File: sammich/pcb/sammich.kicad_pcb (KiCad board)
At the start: 2 copper layers, 34.5 x 25.9 mm, 38 parts, among them J1 Conn_01x02, J2 Conn_02x05_Odd_Even, J3 Conn_01x04, U1 STM32F103RBTx, U2 LD3985M33R_SOT23, U3 MAX485E, Y1 Crystal

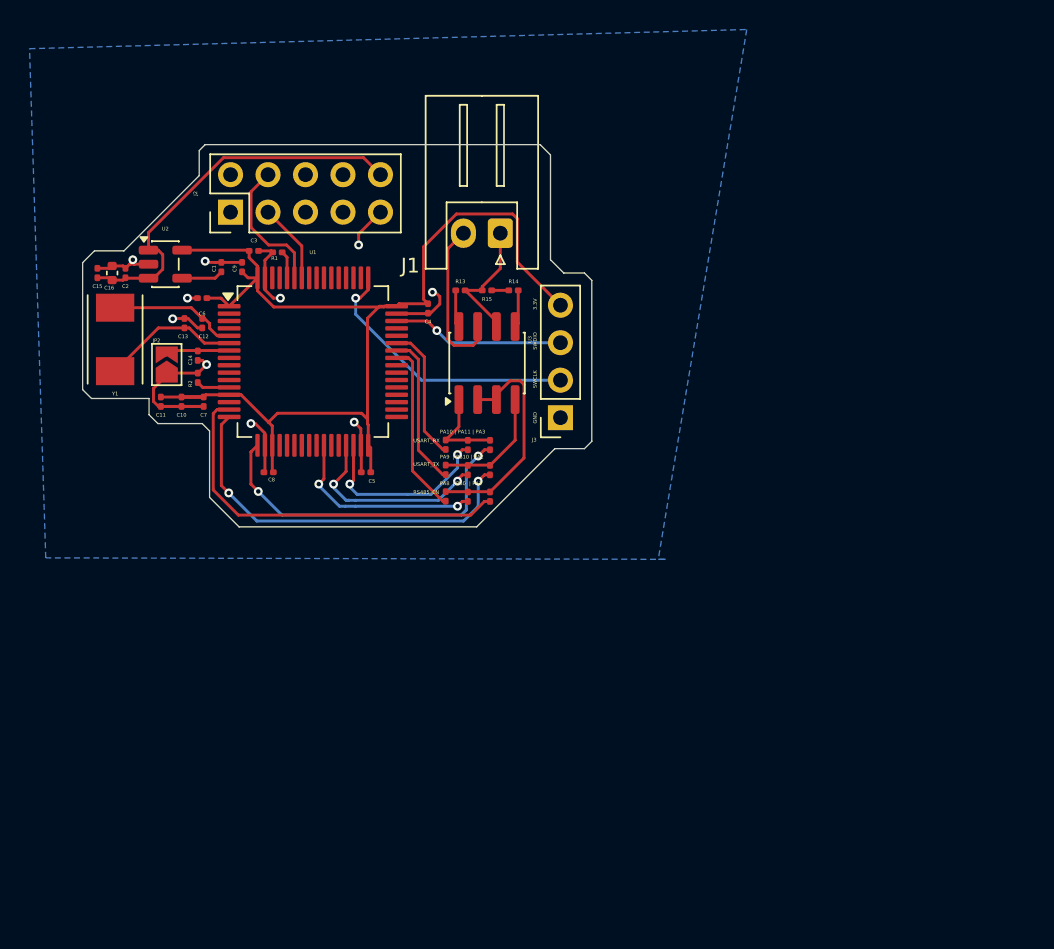
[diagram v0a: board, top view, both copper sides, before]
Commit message: Updated PCB to use I2C
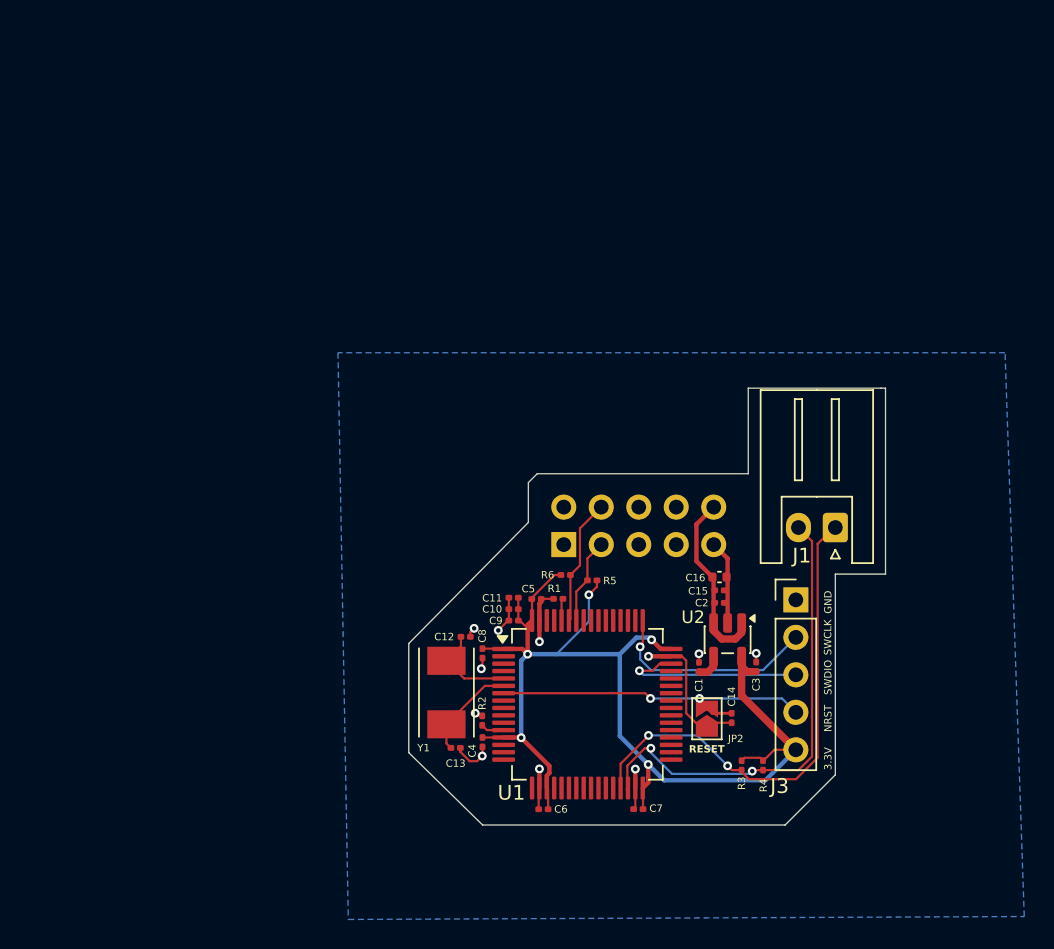
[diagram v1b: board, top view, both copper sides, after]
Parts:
- removed R10, R11, R7, R8, R9: 0, Resistor_SMD:R_0201_0603Metric
- removed R13, R14: 20k, Resistor_SMD:R_0201_0603Metric
- removed R15: 120, Resistor_SMD:R_0201_0603Metric
- removed U3: MAX485E, Package_SO:SOIC-8_3.9x4.9mm_P1.27mm
- J2: footprint Connector_PinHeader_2.54mm:PinHeader_2x05_P2.54mm_Vertical -> Connector_PinSocket_2.54mm:PinSocket_2x05_P2.54mm_Vertical; moved to B.Cu
- J3: value Conn_01x04 -> Conn_01x05; footprint Connector_PinSocket_2.54mm:PinSocket_1x04_P2.54mm_Vertical -> Connector_PinHeader_2.54mm:PinHeader_1x05_P2.54mm_Vertical
- R3, R4, R5, R6: value 0 -> 4.7k
- moved C15 47.3 mm to (87.5, 51.5), turned to 0 degrees
- moved C2 46.0 mm to (87.5, 52.4), turned to 0 degrees
- moved C16 46.0 mm to (87.5, 50.6), turned to 0 degrees
- moved U2 45.8 mm to (88.1, 54.9), turned to -90 degrees
- moved C3 44.2 mm to (90.0, 56.7), turned to 90 degrees
- moved JP2 43.8 mm to (86.7, 60.2)
- moved C14 43.7 mm to (88.4, 60.1)
- moved C1 42.2 mm to (86.2, 56.7)
- moved C6 41.6 mm to (75.6, 66.3)
- moved C7 40.4 mm to (82.0, 66.3), turned to 180 degrees
- moved C13 34.1 mm to (69.7, 62.2), turned to 180 degrees
- moved Y1 32.8 mm to (69.0, 58.4)
- moved J2 31.9 mm to (77.0, 48.4), turned to -90 degrees
- moved J1 30.2 mm to (95.4, 47.2)
- moved R1 30.2 mm to (76.6, 52.1)
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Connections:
- C14 pad 2: Net-(JP2-B) -> NRST
- J1 pad 1: RS485A -> SCL_OUT
- J1 pad 2: RS485B -> SDA_OUT
- J3 pad 4: 3.3V -> NRST
- JP2 pad 2: Net-(JP2-B) -> NRST
- R3 pad 1: PA2 -> SCL_OUT
- R3 pad 2: USART_TX -> 3.3V
- R4 pad 1: PA9 -> SDA_OUT
- R4 pad 2: USART_TX -> 3.3V
- R5 pad 1: PB10 -> SCL
- R5 pad 2: USART_TX -> 3.3V
- R6 pad 1: PA3 -> SDA
- R6 pad 2: USART_RX -> 3.3V
- U1 pad 15: PA1 -> unconnected-(U1-PA1-Pad15)
- U1 pad 16: PA2 -> unconnected-(U1-PA2-Pad16)
- U1 pad 17: PA3 -> unconnected-(U1-PA3-Pad17)
- U1 pad 26: PB0 -> unconnected-(U1-PB0-Pad26)
- U1 pad 29: PB10 -> SCL_OUT
- U1 pad 30: PB11 -> SDA_OUT
- U1 pad 41: PA8 -> unconnected-(U1-PA8-Pad41)
- U1 pad 42: PA9 -> unconnected-(U1-PA9-Pad42)
- U1 pad 43: PA10 -> unconnected-(U1-PA10-Pad43)
- U1 pad 62: PB9 -> unconnected-(U1-PB9-Pad62)
- U1 pad 7: Net-(JP2-B) -> NRST
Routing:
- net SCL_OUT: track 0.00 -> 33.9 mm, vias 0 -> 2
- net SDA_OUT: track 0.00 -> 32.0 mm, vias 0 -> 2
- net PA2: track 26.4 -> 0.00 mm, vias 2 -> 0
- net PA1: track 26.2 -> 0.00 mm
- net PA3: track 23.5 -> 0.00 mm, vias 2 -> 0
- net NRST: track 0.00 -> 23.0 mm, vias 0 -> 2
- net 5V: track 28.9 -> 12.3 mm
- net RS485_EN: track 15.2 -> 0.00 mm
- net PB0: track 13.8 -> 0.00 mm, vias 2 -> 0
- net PB10: track 13.4 -> 0.00 mm, vias 2 -> 0
- net PB11: track 12.9 -> 0.00 mm, vias 2 -> 0
- net RS485B: track 12.1 -> 0.00 mm
- net GND: track 45.7 -> 33.7 mm, vias 10 -> 11
- net PA8: track 11.7 -> 0.00 mm
- net PA9: track 10.4 -> 0.00 mm
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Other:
- board size 34.5 x 25.9 mm -> 32.3 x 29.6 mm
- board text added: "Kapto PnP Sammich v1.0"
- board text added: "NRST"
- board text added: "RESET"
- board text removed: "Isaac Lonergan"
- board text removed: "PA10 | PA11 | PA3"
- board text removed: "PA8 | PB0 | PA1"
- board text removed: "PA9 | PB10 | PA2"
- board text removed: "RS485_EN"
- board text removed: "USART_RX"
- board text removed: "USART_TX"
